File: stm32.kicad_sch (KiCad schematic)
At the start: 11 parts, among them U1 STM32H743VGTx, Y2 LFXTAL078719Cutt

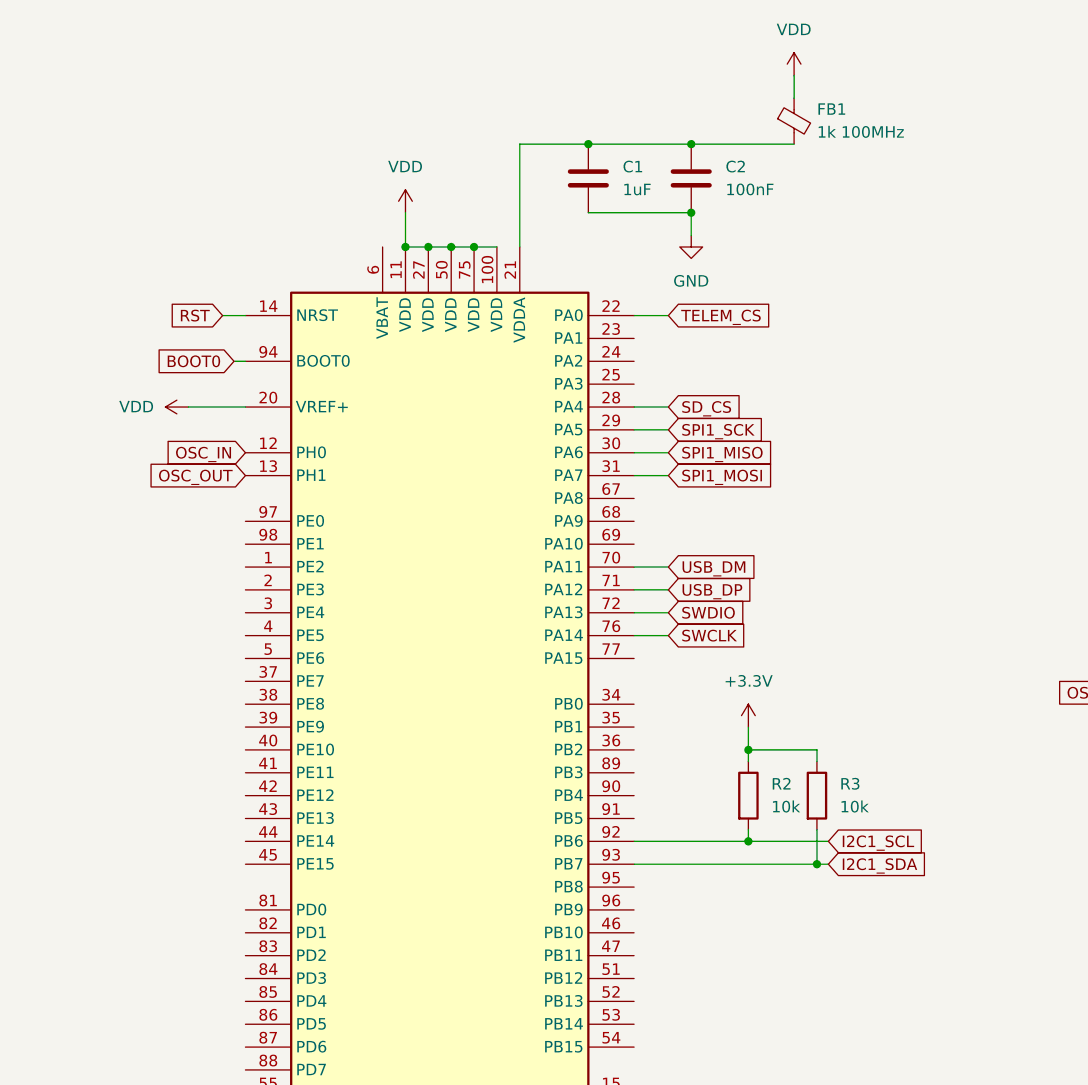
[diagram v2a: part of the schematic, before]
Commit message: Change 0201 to 0403
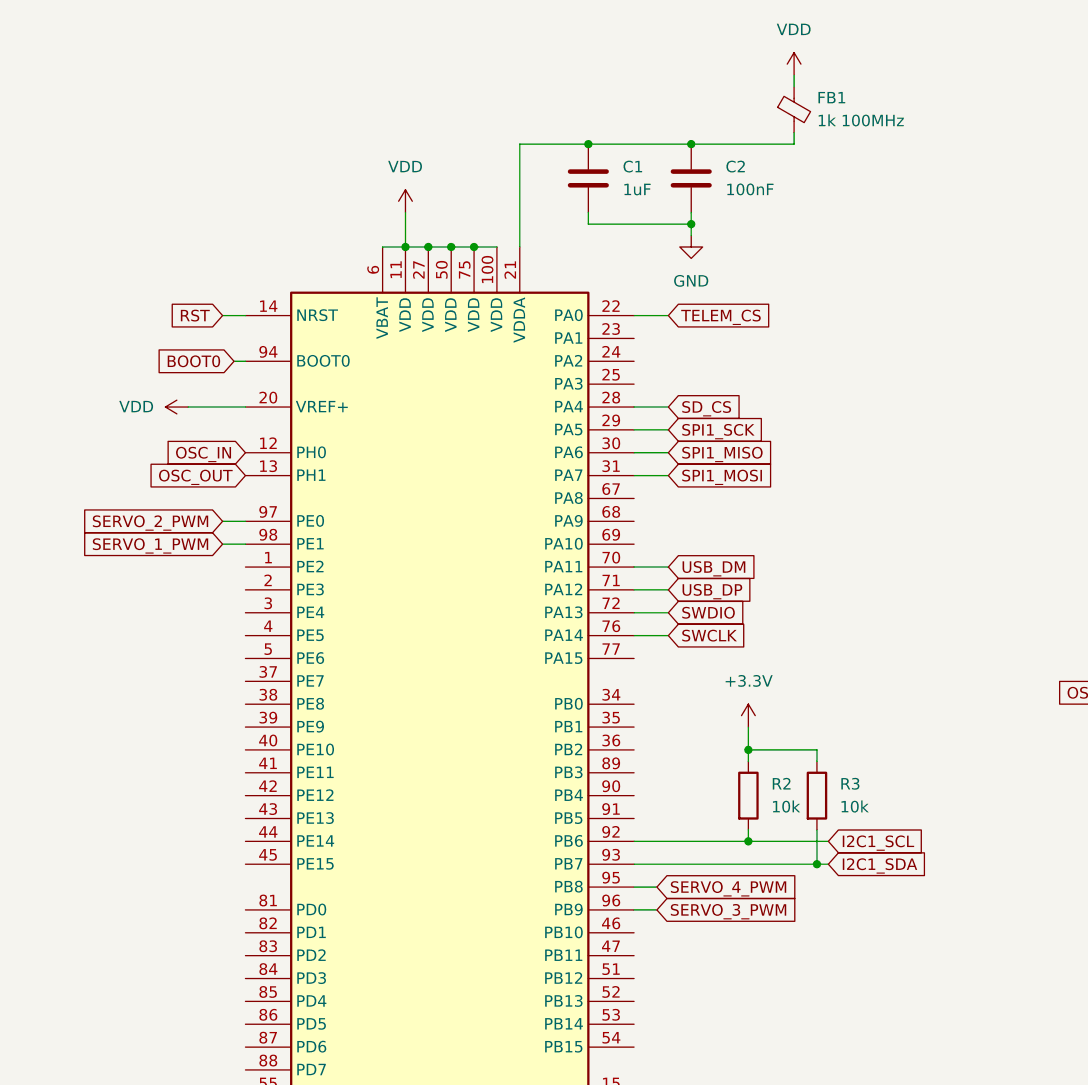
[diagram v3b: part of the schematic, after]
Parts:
- C1, C14, C15, C2: footprint Capacitor_SMD:C_0201_0603Metric -> Capacitor_SMD:C_0402_1005Metric
- FB1: footprint Capacitor_SMD:C_0201_0603Metric -> Capacitor_SMD:C_0603_1608Metric
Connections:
- net VDD: now also U1.6 (VBAT)
- net SERVO_4_PWM: now reaches U1.95 (PB8)
- net SERVO_3_PWM: now reaches U1.96 (PB9)
- net SERVO_2_PWM: now reaches U1.97 (PE0)
- net SERVO_1_PWM: now reaches U1.98 (PE1)
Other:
- moved on the sheet: FB1
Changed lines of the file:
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@@
-	)
-	(junction
-		(at 158.75 38.1)
-		(diameter 0)
-		(color 0 0 0 0)
 	)
 	(junction
@@
 	)
 	(junction
+		(at 158.75 39.37)
+		(diameter 0)
+		(color 0 0 0 0)
+	)
+	(junction
 		(at 132.08 41.91)
 		(diameter 0)
@@
 	(wire
 		(pts
+			(xy 124.46 41.91) (xy 127 41.91)
+		)
+		(stroke
+			(width 0)
+			(type default)
+		)
+	)
+	(wire
+		(pts
 			(xy 99.06 158.75) (xy 86.36 158.75)
 		)
@@
 	(wire
 		(pts
+			(xy 147.32 39.37) (xy 147.32 38.1)
+		)
+		(stroke
+			(width 0)
+			(type default)
+		)
+	)
+	(wire
+		(pts
 			(xy 213.36 99.06) (xy 241.3 99.06)
 		)
@@
 	(wire
 		(pts
-			(xy 158.75 30.48) (xy 170.18 30.48)
+			(xy 106.68 72.39) (xy 109.22 72.39)
 		)
 		(stroke
@@
 	(wire
 		(pts
-			(xy 170.18 22.86) (xy 170.18 25.4)
+			(xy 170.18 22.86) (xy 170.18 24.13)
 		)
 		(stroke
@@
 	(wire
 		(pts
-			(xy 158.75 38.1) (xy 158.75 40.64)
+			(xy 158.75 38.1) (xy 158.75 39.37)
 		)
 		(stroke
@@
 	(wire
 		(pts
-			(xy 147.32 38.1) (xy 158.75 38.1)
+			(xy 170.18 30.48) (xy 158.75 30.48)
+		)
+		(stroke
+			(width 0)
+			(type default)
+		)
+	)
+	(wire
+		(pts
+			(xy 147.32 39.37) (xy 158.75 39.37)
+		)
+		(stroke
+			(width 0)
+			(type default)
+		)
+	)
+	(wire
+		(pts
+			(xy 170.18 29.21) (xy 170.18 30.48)
+		)
+		(stroke
+			(width 0)
+			(type default)
+		)
+	)
+	(wire
+		(pts
+			(xy 152.4 113.03) (xy 154.94 113.03)
 		)
 		(stroke
@@
 	(wire
 		(pts
+			(xy 106.68 74.93) (xy 109.22 74.93)
+		)
+		(stroke
+			(width 0)
+			(type default)
+		)
+	)
+	(wire
+		(pts
 			(xy 165.1 106.68) (xy 165.1 107.95)
 		)
@@
 	(wire
 		(pts
+			(xy 158.75 39.37) (xy 158.75 40.64)
+		)
+		(stroke
+			(width 0)
+			(type default)
+		)
+	)
+	(wire
+		(pts
 			(xy 270.51 88.9) (xy 270.51 90.17)
 		)
@@
 			(width 0)
 			(type default)
+		)
+	)
+	(wire
+		(pts
+			(xy 152.4 115.57) (xy 154.94 115.57)
+		)
+		(stroke
+			(width 0)
+			(type default)
+		)
+	)
+	(global_label "SERVO_2_PWM"
+		(shape input)
+		(at 106.68 72.39 180)
+		(fields_autoplaced yes)
+		(effects
+			(font
+				(size 1.27 1.27)
+			)
+			(justify right)
+		)
+		(property "Intersheetrefs" "${INTERSHEET_REFS}"
+			(at 90.3297 72.39 0)
+			(effects
+				(font
+					(size 1.27 1.27)
+				)
+				(justify right)
+				(hide yes)
+			)
 		)
 	)
@@
 		)
 	)
+	(global_label "SERVO_3_PWM"
+		(shape input)
+		(at 154.94 115.57 0)
+		(fields_autoplaced yes)
+		(effects
+			(font
+				(size 1.27 1.27)
+			)
+			(justify left)
+		)
+		(property "Intersheetrefs" "${INTERSHEET_REFS}"
+			(at 171.2903 115.57 0)
+			(effects
+				(font
+					(size 1.27 1.27)
+				)
+				(justify left)
+				(hide yes)
+			)
+		)
+	)
 	(global_label "USB_DP"
 		(shape input)
@@
 		)
 	)
+	(global_label "SERVO_4_PWM"
+		(shape input)
+		(at 154.94 113.03 0)
+		(fields_autoplaced yes)
+		(effects
+			(font
+				(size 1.27 1.27)
+			)
+			(justify left)
+		)
+		(property "Intersheetrefs" "${INTERSHEET_REFS}"
+			(at 171.2903 113.03 0)
+			(effects
+				(font
+					(size 1.27 1.27)
+				)
+				(justify left)
+				(hide yes)
+			)
+		)
+	)
 	(global_label "I2C1_SDA"
 		(shape input)
@@
 				)
 				(justify left)
+				(hide yes)
+			)
+		)
+	)
+	(global_label "SERVO_1_PWM"
+		(shape input)
+		(at 106.68 74.93 180)
+		(fields_autoplaced yes)
+		(effects
+			(font
+				(size 1.27 1.27)
+			)
+			(justify right)
+		)
+		(property "Intersheetrefs" "${INTERSHEET_REFS}"
+			(at 90.3297 74.93 0)
+			(effects
+				(font
+					(size 1.27 1.27)
+				)
+				(justify right)
 				(hide yes)
 			)
@@
 			)
 		)
-		(property "Footprint" "Capacitor_SMD:C_0201_0603Metric"
+		(property "Footprint" "Capacitor_SMD:C_0402_1005Metric"
 			(at 159.7152 38.1 0)
 			(effects
@@
 	(symbol
 		(lib_id "Device:FerriteBead_Small")
-		(at 170.18 27.94 0)
+		(at 170.18 26.67 0)
 		(unit 1)
 		(exclude_from_sim no)
@@
 		(fields_autoplaced yes)
 		(property "Reference" "FB1"
-			(at 172.72 26.6318 0)
+			(at 172.72 25.3618 0)
 			(effects
 				(font
@@
 		)
 		(property "Value" "1k 100MHz"
-			(at 172.72 29.1718 0)
-			(effects
-				(font
-					(size 1.27 1.27)
-				)
-				(justify left)
-			)
-		)
-		(property "Footprint" "Capacitor_SMD:C_0201_0603Metric"
-			(at 168.402 27.94 90)
+			(at 172.72 27.9018 0)
+			(effects
+				(font
+					(size 1.27 1.27)
+				)
+				(justify left)
+			)
+		)
+		(property "Footprint" "Capacitor_SMD:C_0603_1608Metric"
+			(at 168.402 26.67 90)
 			(effects
 				(font
@@
 		)
 		(property "Datasheet" "https://www.mouser.com/datasheet/2/281/ENFA0004-1915711.pdf"
-			(at 170.18 27.94 0)
+			(at 170.18 26.67 0)
 			(effects
 				(font
@@
 		)
 		(property "Description" "Ferrite bead, small symbol"
-			(at 170.18 27.94 0)
+			(at 170.18 26.67 0)
 			(effects
 				(font
@@
 			)
 		)
-		(property "Footprint" "Capacitor_SMD:C_0201_0603Metric"
+		(property "Footprint" "Capacitor_SMD:C_0402_1005Metric"
 			(at 87.3252 168.91 0)
 			(effects
@@
 			)
 		)
-		(property "Footprint" "Capacitor_SMD:C_0201_0603Metric"
+		(property "Footprint" "Capacitor_SMD:C_0402_1005Metric"
 			(at 148.2852 38.1 0)
 			(effects
@@
 			)
 		)
-		(property "Footprint" "Capacitor_SMD:C_0201_0603Metric"
+		(property "Footprint" "Capacitor_SMD:C_0402_1005Metric"
 			(at 100.0252 168.91 0)
 			(effects

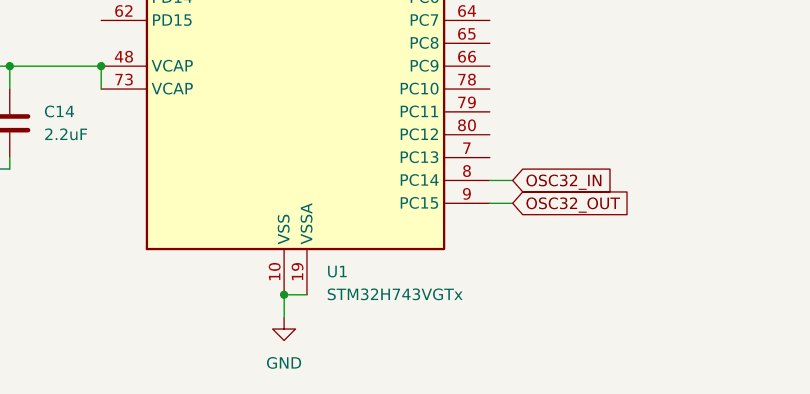
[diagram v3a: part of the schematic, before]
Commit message: Added STM32_MX Project, LED, Fixed DRC Violations
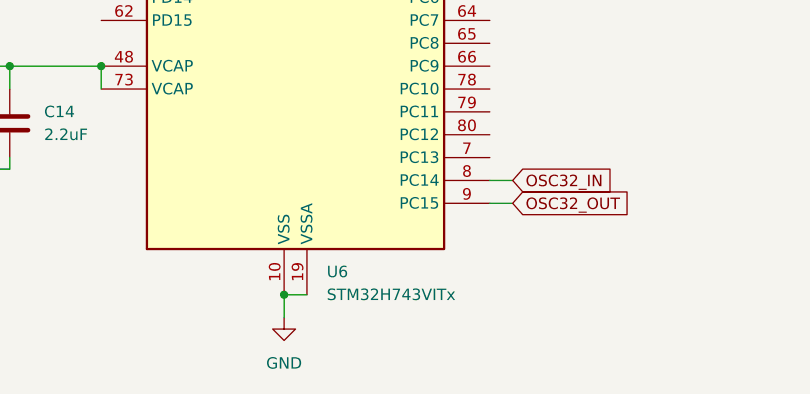
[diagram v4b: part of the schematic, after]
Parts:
- removed U1: STM32H743VGTx, Package_QFP:LQFP-100_14x14mm_P0.5mm, symbol MCU_ST_STM32H7:STM32H743VGTx
- added U6: STM32H743VITx, Package_QFP:LQFP-100_14x14mm_P0.5mm, symbol MCU_ST_STM32H7:STM32H743VITx
- Y2: footprint LFXTAL078719Cutt -> VanguardLib:LFXTAL078719Cutt
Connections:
- net BOOT0: now also U6.94 (BOOT0)
- net GND: now also U6.10 (VSS), U6.19 (VSSA), U6.26 (VSS), U6.49 (VSS), U6.74 (VSS), U6.99 (VSS)
- net I2C1_SCL: now also U6.92 (PB6)
- net I2C1_SDA: now also U6.93 (PB7)
- net OSC32_IN: now also U6.8 (PC14)
- net OSC32_OUT: now also U6.9 (PC15)
- net OSC_IN: now also U6.12 (PH0)
- net OSC_OUT: now also U6.13 (PH1)
- net RST: now also U6.14 (NRST)
- net SD_CS: now also U6.28 (PA4)
- net SERVO_1_PWM: now also U6.98 (PE1)
- net SERVO_2_PWM: now also U6.97 (PE0)
- net SERVO_3_PWM: now also U6.96 (PB9)
- net SERVO_4_PWM: now also U6.95 (PB8)
- net SPI1_MISO: now also U6.30 (PA6)
- net SPI1_MOSI: now also U6.31 (PA7)
- net SPI1_SCK: now also U6.29 (PA5)
- net SWCLK: now also U6.76 (PA14)
- net SWDIO: now also U6.72 (PA13)
- net TELEM_CS: now also U6.22 (PA0)
- net USB_DM: now also U6.70 (PA11)
- net USB_DP: now also U6.71 (PA12)
- net VDD: now also U6.100 (VDD), U6.11 (VDD), U6.20 (VREF+), U6.27 (VDD), U6.50 (VDD), U6.6 (VBAT), U6.75 (VDD)
- net at C1.1, C2.1, FB1.2: now also U6.21 (VDDA)
- net at C14.1, C15.1: now also U6.48 (VCAP), U6.73 (VCAP)
